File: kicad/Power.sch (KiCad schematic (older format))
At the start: 11 parts, among them P3 Battery, U3 LXDC2URxx

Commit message: 自動配線成功
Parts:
- P3: footprint Connectors_Hirose:Hirose_DF13-02P-1.25DSA_02x1.25mm_Straight -> mouse:Hirose_DF13-02P-1.25DSA_02x1.25mm_Straight
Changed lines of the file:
@@
 F 0 "P3" H 1700 4600 50  0000 C CNN
 F 1 "Battery" V 1800 4450 50  0000 C CNN
-F 2 "Connectors_Hirose:Hirose_DF13-02P-1.25DSA_02x1.25mm_Straight" H 1700 4450 50  0001 C CNN
+F 2 "mouse:Hirose_DF13-02P-1.25DSA_02x1.25mm_Straight" H 1700 4450 50  0001 C CNN
 F 3 "" H 1700 4450 50  0000 C CNN
 	1    1700 4450

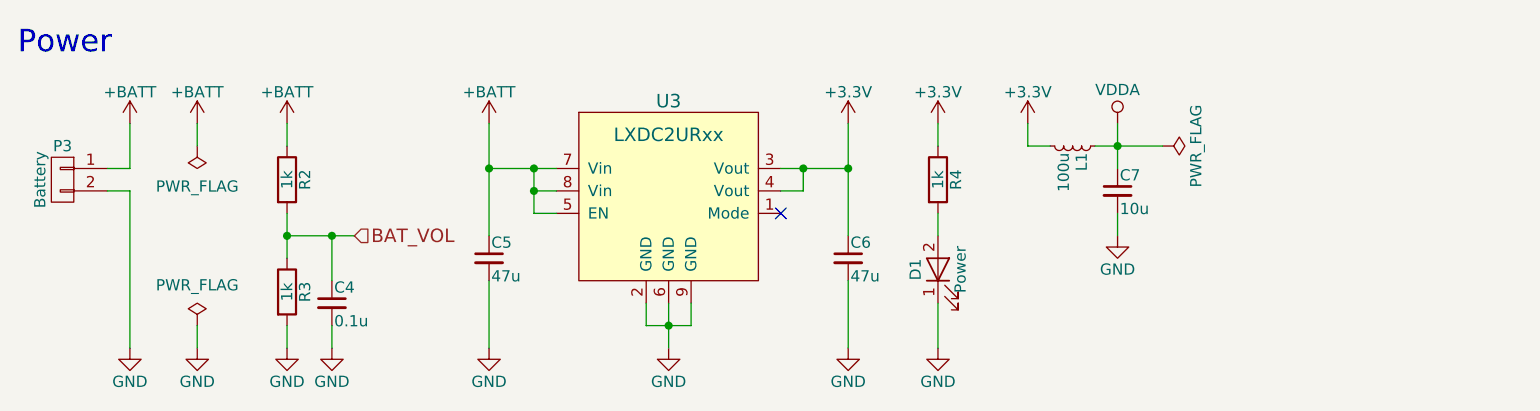
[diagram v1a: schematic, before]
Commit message: 回路を改良
受光部をフォトトランジスタに変更
測距センサをVL6180Xに変更
動作電圧を3Vに変更
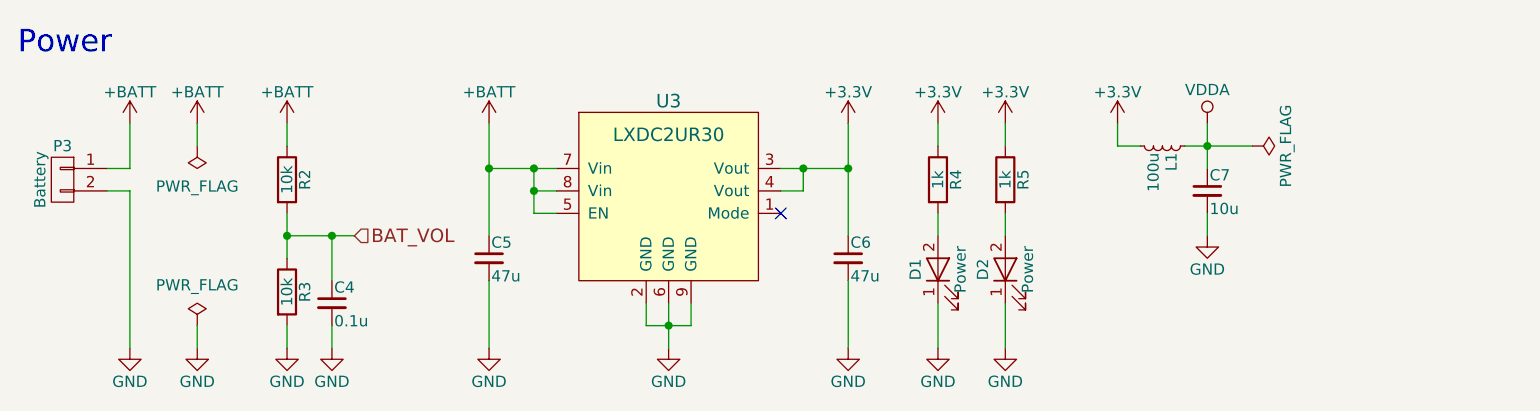
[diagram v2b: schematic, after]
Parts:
- added D2: Power, LEDs:LED_0402, symbol LED
- added R5: 1k, Resistors_SMD:R_0201, symbol R
- R2, R3: value 1k -> 10k
- U3: value LXDC2URxx -> LXDC2UR30
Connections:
- net +3V3: now also R5.1
- net GND: now also D2.1 (K)
- new net: D2.2 (A), R5.2
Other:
- moved on the sheet: C7, L1
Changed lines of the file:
@@
 LIBS:ftdi
 LIBS:gennum
-LIBS:graphic
 LIBS:hc11
 LIBS:ir
 LIBS:Lattice
 LIBS:leds
-LIBS:logo
 LIBS:maxim
 LIBS:mechanical
@@
 LIBS:zetex
 LIBS:Zilog
+LIBS:graphic_symbols
+LIBS:infineon
+LIBS:intersil
+LIBS:LEM
+LIBS:logic_programmable
+LIBS:RFSolutions
 LIBS:KERISE-cache
 EELAYER 25 0
@@
 P 2700 4450
 F 0 "R2" V 2780 4450 50  0000 C CNN
-F 1 "1k" V 2700 4450 50  0000 C CNN
+F 1 "10k" V 2700 4450 50  0000 C CNN
 F 2 "Resistors_SMD:R_0201" V 2630 4450 50  0001 C CNN
 F 3 "" H 2700 4450 50  0000 C CNN
@@
 P 2700 4950
 F 0 "R3" V 2780 4950 50  0000 C CNN
-F 1 "1k" V 2700 4950 50  0000 C CNN
+F 1 "10k" V 2700 4950 50  0000 C CNN
 F 2 "Resistors_SMD:R_0201" V 2630 4950 50  0001 C CNN
 F 3 "" H 2700 4950 50  0000 C CNN
@@
 P 4400 4250
 F 0 "U3" H 4400 4400 60  0000 C CNN
-F 1 "LXDC2URxx" H 4400 4250 60  0000 C CNN
+F 1 "LXDC2UR30" H 4400 4250 60  0000 C CNN
 F 2 "mouse:LXDC2UR" H 4400 4250 60  0001 C CNN
 F 3 "" H 4400 4250 60  0000 C CNN
@@
 L +3.3V #PWR031
 U 1 1 59C37023
-P 6000 4200
-F 0 "#PWR031" H 6000 4050 50  0001 C CNN
-F 1 "+3.3V" H 6000 4340 50  0000 C CNN
-F 2 "" H 6000 4200 50  0001 C CNN
-F 3 "" H 6000 4200 50  0001 C CNN
-	1    6000 4200
-	1    0    0    -1
-$EndComp
-$Comp
-L VDDA #PWR032
-U 1 1 59C37047
 P 6400 4200
-F 0 "#PWR032" H 6400 4050 50  0001 C CNN
-F 1 "VDDA" H 6400 4350 50  0000 C CNN
+F 0 "#PWR031" H 6400 4050 50  0001 C CNN
+F 1 "+3.3V" H 6400 4340 50  0000 C CNN
 F 2 "" H 6400 4200 50  0001 C CNN
 F 3 "" H 6400 4200 50  0001 C CNN
@@
 $EndComp
 $Comp
+L VDDA #PWR032
+U 1 1 59C37047
+P 6800 4200
+F 0 "#PWR032" H 6800 4050 50  0001 C CNN
+F 1 "VDDA" H 6800 4350 50  0000 C CNN
+F 2 "" H 6800 4200 50  0001 C CNN
+F 3 "" H 6800 4200 50  0001 C CNN
+	1    6800 4200
+	1    0    0    -1
+$EndComp
+$Comp
 L L_Small L1
 U 1 1 59C3706B
-P 6200 4300
-F 0 "L1" H 6230 4340 50  0000 L CNN
-F 1 "100u" H 6230 4260 50  0000 L CNN
-F 2 "Capacitors_SMD:C_0603" H 6200 4300 50  0001 C CNN
-F 3 "" H 6200 4300 50  0001 C CNN
-	1    6200 4300
+P 6600 4300
+F 0 "L1" H 6630 4340 50  0000 L CNN
+F 1 "100u" H 6630 4260 50  0000 L CNN
+F 2 "Capacitors_SMD:C_0603" H 6600 4300 50  0001 C CNN
+F 3 "" H 6600 4300 50  0001 C CNN
+	1    6600 4300
 	0    1    1    0
 $EndComp
@@
 L C_Small C7
 U 1 1 59C370C1
-P 6400 4500
-F 0 "C7" H 6410 4570 50  0000 L CNN
-F 1 "10u" H 6410 4420 50  0000 L CNN
-F 2 "Capacitors_SMD:C_0402" H 6400 4500 50  0001 C CNN
-F 3 "" H 6400 4500 50  0001 C CNN
-	1    6400 4500
-	1    0    0    -1
-$EndComp
-Wire Wire Line
-	6400 4200 6400 4400
+P 6800 4500
+F 0 "C7" H 6810 4570 50  0000 L CNN
+F 1 "10u" H 6810 4420 50  0000 L CNN
+F 2 "Capacitors_SMD:C_0402" H 6800 4500 50  0001 C CNN
+F 3 "" H 6800 4500 50  0001 C CNN
+	1    6800 4500
+	1    0    0    -1
+$EndComp
+Wire Wire Line
+	6800 4200 6800 4400
 $Comp
 L GND #PWR033
 U 1 1 59C37170
-P 6400 4700
-F 0 "#PWR033" H 6400 4450 50  0001 C CNN
-F 1 "GND" H 6400 4550 50  0000 C CNN
-F 2 "" H 6400 4700 50  0000 C CNN
-F 3 "" H 6400 4700 50  0000 C CNN
-	1    6400 4700
-	1    0    0    -1
-$EndComp
-Wire Wire Line
-	6400 4700 6400 4600
-Wire Wire Line
-	6300 4300 6600 4300
-Connection ~ 6400 4300
-Wire Wire Line
-	6100 4300 6000 4300
-Wire Wire Line
-	6000 4300 6000 4200
+P 6800 4700
+F 0 "#PWR033" H 6800 4450 50  0001 C CNN
+F 1 "GND" H 6800 4550 50  0000 C CNN
+F 2 "" H 6800 4700 50  0000 C CNN
+F 3 "" H 6800 4700 50  0000 C CNN
+	1    6800 4700
+	1    0    0    -1
+$EndComp
+Wire Wire Line
+	6800 4700 6800 4600
+Wire Wire Line
+	6700 4300 7000 4300
+Connection ~ 6800 4300
+Wire Wire Line
+	6500 4300 6400 4300
+Wire Wire Line
+	6400 4300 6400 4200
 $Comp
 L C_Small C5
@@
 L PWR_FLAG #FLG035
 U 1 1 5A1BE075
-P 6600 4300
-F 0 "#FLG035" H 6600 4375 50  0001 C CNN
-F 1 "PWR_FLAG" H 6600 4450 50  0000 C CNN
-F 2 "" H 6600 4300 50  0001 C CNN
-F 3 "" H 6600 4300 50  0001 C CNN
-	1    6600 4300
+P 7000 4300
+F 0 "#FLG035" H 7000 4375 50  0001 C CNN
+F 1 "PWR_FLAG" H 7000 4450 50  0000 C CNN
+F 2 "" H 7000 4300 50  0001 C CNN
+F 3 "" H 7000 4300 50  0001 C CNN
+	1    7000 4300
 	0    1    1    0
 $EndComp
+$Comp
+L R R5
+U 1 1 5A4BB521
+P 5900 4450
+F 0 "R5" V 5980 4450 50  0000 C CNN
+F 1 "1k" V 5900 4450 50  0000 C CNN
+F 2 "Resistors_SMD:R_0201" V 5830 4450 50  0001 C CNN
+F 3 "" H 5900 4450 50  0000 C CNN
+	1    5900 4450
+	1    0    0    -1
+$EndComp
+$Comp
+L GND #PWR036
+U 1 1 5A4BB527
+P 5900 5200
+F 0 "#PWR036" H 5900 4950 50  0001 C CNN
+F 1 "GND" H 5900 5050 50  0000 C CNN
+F 2 "" H 5900 5200 50  0000 C CNN
+F 3 "" H 5900 5200 50  0000 C CNN
+	1    5900 5200
+	1    0    0    -1
+$EndComp
+$Comp
+L +3.3V #PWR037
+U 1 1 5A4BB52D
+P 5900 4200
+F 0 "#PWR037" H 5900 4050 50  0001 C CNN
+F 1 "+3.3V" H 5900 4340 50  0000 C CNN
+F 2 "" H 5900 4200 50  0000 C CNN
+F 3 "" H 5900 4200 50  0000 C CNN
+	1    5900 4200
+	1    0    0    -1
+$EndComp
+Wire Wire Line
+	5900 4700 5900 4600
+Wire Wire Line
+	5900 4300 5900 4200
+$Comp
+L LED D2
+U 1 1 5A4BB535
+P 5900 4850
+F 0 "D2" H 5900 4950 50  0000 C CNN
+F 1 "Power" H 5900 4750 50  0000 C CNN
+F 2 "LEDs:LED_0402" H 5900 4850 50  0001 C CNN
+F 3 "" H 5900 4850 50  0001 C CNN
+	1    5900 4850
+	0    -1   -1   0
+$EndComp
+Wire Wire Line
+	5900 5000 5900 5200
 $EndSCHEMATC

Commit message: 部品を配置
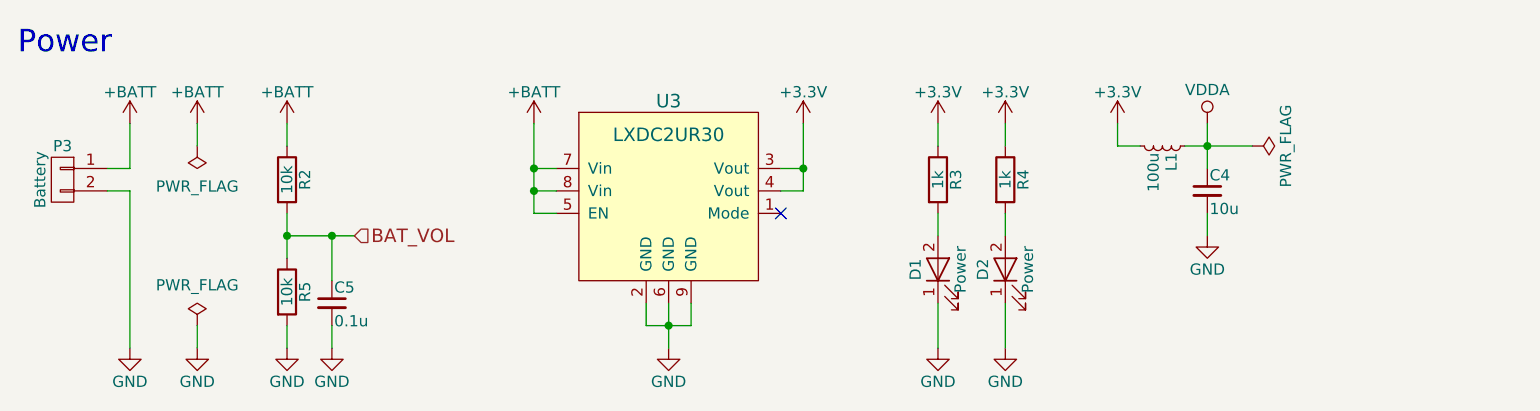
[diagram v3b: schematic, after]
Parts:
- removed C5, C6: 47u, Capacitors_SMD:C_0805, symbol C_Small
- C4: renamed from C7; footprint Capacitors_SMD:C_0402 -> Capacitors_SMD:C_0402_NoSilk
- C5: renamed from C4; footprint Capacitors_SMD:C_0201 -> Capacitors_SMD:C_0201_NoSilk
- R2: footprint Resistors_SMD:R_0201 -> Resistors_SMD:R_0201_NoSilk
- R3: renamed from R4; footprint Resistors_SMD:R_0201 -> Resistors_SMD:R_0201_NoSilk
- R4: renamed from R5; footprint Resistors_SMD:R_0201 -> Resistors_SMD:R_0201_NoSilk
- R5: renamed from R3; footprint Resistors_SMD:R_0201 -> Resistors_SMD:R_0201_NoSilk
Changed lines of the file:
@@
 $Descr A4 11693 8268
 encoding utf-8
-Sheet 3 15
+Sheet 3 16
 Title ""
 Date ""
@@
 F 0 "R2" V 2780 4450 50  0000 C CNN
 F 1 "10k" V 2700 4450 50  0000 C CNN
-F 2 "Resistors_SMD:R_0201" V 2630 4450 50  0001 C CNN
+F 2 "Resistors_SMD:R_0201_NoSilk" V 2630 4450 50  0001 C CNN
 F 3 "" H 2700 4450 50  0000 C CNN
 	1    2700 4450
@@
 $EndComp
 $Comp
-L R R3
+L R R5
 U 1 1 57CD3B95
 P 2700 4950
-F 0 "R3" V 2780 4950 50  0000 C CNN
+F 0 "R5" V 2780 4950 50  0000 C CNN
 F 1 "10k" V 2700 4950 50  0000 C CNN
-F 2 "Resistors_SMD:R_0201" V 2630 4950 50  0001 C CNN
+F 2 "Resistors_SMD:R_0201_NoSilk" V 2630 4950 50  0001 C CNN
 F 3 "" H 2700 4950 50  0000 C CNN
 	1    2700 4950
@@
 $EndComp
 $Comp
-L R R4
+L R R3
 U 1 1 57D00960
 P 5600 4450
-F 0 "R4" V 5680 4450 50  0000 C CNN
+F 0 "R3" V 5680 4450 50  0000 C CNN
 F 1 "1k" V 5600 4450 50  0000 C CNN
-F 2 "Resistors_SMD:R_0201" V 5530 4450 50  0001 C CNN
+F 2 "Resistors_SMD:R_0201_NoSilk" V 5530 4450 50  0001 C CNN
 F 3 "" H 5600 4450 50  0000 C CNN
 	1    5600 4450
@@
 L +BATT #PWR025
 U 1 1 592A5000
-P 3600 4200
-F 0 "#PWR025" H 3600 4050 50  0001 C CNN
-F 1 "+BATT" H 3600 4340 50  0000 C CNN
-F 2 "" H 3600 4200 50  0000 C CNN
-F 3 "" H 3600 4200 50  0000 C CNN
-	1    3600 4200
+P 3800 4200
+F 0 "#PWR025" H 3800 4050 50  0001 C CNN
+F 1 "+BATT" H 3800 4340 50  0000 C CNN
+F 2 "" H 3800 4200 50  0000 C CNN
+F 3 "" H 3800 4200 50  0000 C CNN
+	1    3800 4200
 	1    0    0    -1
 $EndComp
@@
 L +3.3V #PWR027
 U 1 1 592A5664
-P 5200 4200
-F 0 "#PWR027" H 5200 4050 50  0001 C CNN
-F 1 "+3.3V" H 5200 4340 50  0000 C CNN
-F 2 "" H 5200 4200 50  0000 C CNN
-F 3 "" H 5200 4200 50  0000 C CNN
-	1    5200 4200
+P 5000 4200
+F 0 "#PWR027" H 5000 4050 50  0001 C CNN
+F 1 "+3.3V" H 5000 4340 50  0000 C CNN
+F 2 "" H 5000 4200 50  0000 C CNN
+F 3 "" H 5000 4200 50  0000 C CNN
+	1    5000 4200
 	1    0    0    -1
 $EndComp
 NoConn ~ 4900 4600
 $Comp
-L C_Small C6
-U 1 1 592A5C4A
-P 5200 4800
-F 0 "C6" H 5210 4870 50  0000 L CNN
-F 1 "47u" H 5210 4720 50  0000 L CNN
-F 2 "Capacitors_SMD:C_0805" H 5200 4800 50  0001 C CNN
-F 3 "" H 5200 4800 50  0000 C CNN
-	1    5200 4800
-	1    0    0    -1
-$EndComp
-$Comp
 L GND #PWR028
-U 1 1 592A5C9B
-P 5200 5200
-F 0 "#PWR028" H 5200 4950 50  0001 C CNN
-F 1 "GND" H 5200 5050 50  0000 C CNN
-F 2 "" H 5200 5200 50  0000 C CNN
-F 3 "" H 5200 5200 50  0000 C CNN
-	1    5200 5200
-	1    0    0    -1
-$EndComp
-$Comp
-L GND #PWR029
 U 1 1 57CC113A
 P 2000 5200
-F 0 "#PWR029" H 2000 4950 50  0001 C CNN
+F 0 "#PWR028" H 2000 4950 50  0001 C CNN
 F 1 "GND" H 2000 5050 50  0000 C CNN
 F 2 "" H 2000 5200 50  0000 C CNN
@@
 	2000 4400 1900 4400
 Wire Wire Line
-	3600 4400 3900 4400
-Wire Wire Line
-	3600 4200 3600 4700
-Wire Wire Line
 	3900 4500 3800 4500
 Wire Wire Line
-	3800 4400 3800 4600
+	3800 4200 3800 4600
 Connection ~ 3800 4400
 Wire Wire Line
@@
 	4500 5100 4500 5000
 Wire Wire Line
-	5200 4200 5200 4700
-Wire Wire Line
-	4900 4400 5200 4400
-Wire Wire Line
-	4900 4500 5000 4500
-Wire Wire Line
-	5000 4500 5000 4400
+	5000 4500 4900 4500
+Wire Wire Line
+	5000 4200 5000 4500
 Connection ~ 5000 4400
 Wire Wire Line
-	5200 5200 5200 4900
-Connection ~ 5200 4400
-Wire Wire Line
 	2000 4200 2000 4400
-$Comp
-L GND #PWR030
-U 1 1 593DFA5D
-P 3600 5200
-F 0 "#PWR030" H 3600 4950 50  0001 C CNN
-F 1 "GND" H 3600 5050 50  0000 C CNN
-F 2 "" H 3600 5200 50  0000 C CNN
-F 3 "" H 3600 5200 50  0000 C CNN
-	1    3600 5200
-	1    0    0    -1
-$EndComp
-Wire Wire Line
-	3600 5200 3600 4900
-Connection ~ 3600 4400
 $Comp
 L LED D1
@@
 	5600 5000 5600 5200
 $Comp
-L +3.3V #PWR031
+L +3.3V #PWR029
 U 1 1 59C37023
 P 6400 4200
-F 0 "#PWR031" H 6400 4050 50  0001 C CNN
+F 0 "#PWR029" H 6400 4050 50  0001 C CNN
 F 1 "+3.3V" H 6400 4340 50  0000 C CNN
 F 2 "" H 6400 4200 50  0001 C CNN
@@
 $EndComp
 $Comp
-L VDDA #PWR032
+L VDDA #PWR030
 U 1 1 59C37047
 P 6800 4200
-F 0 "#PWR032" H 6800 4050 50  0001 C CNN
+F 0 "#PWR030" H 6800 4050 50  0001 C CNN
 F 1 "VDDA" H 6800 4350 50  0000 C CNN
 F 2 "" H 6800 4200 50  0001 C CNN
@@
 $EndComp
 $Comp
-L C_Small C7
+L C_Small C4
 U 1 1 59C370C1
 P 6800 4500
-F 0 "C7" H 6810 4570 50  0000 L CNN
+F 0 "C4" H 6810 4570 50  0000 L CNN
 F 1 "10u" H 6810 4420 50  0000 L CNN
-F 2 "Capacitors_SMD:C_0402" H 6800 4500 50  0001 C CNN
+F 2 "Capacitors_SMD:C_0402_NoSilk" H 6800 4500 50  0001 C CNN
 F 3 "" H 6800 4500 50  0001 C CNN
 	1    6800 4500
@@
 	6800 4200 6800 4400
 $Comp
-L GND #PWR033
+L GND #PWR031
 U 1 1 59C37170
 P 6800 4700
-F 0 "#PWR033" H 6800 4450 50  0001 C CNN
+F 0 "#PWR031" H 6800 4450 50  0001 C CNN
 F 1 "GND" H 6800 4550 50  0000 C CNN
 F 2 "" H 6800 4700 50  0000 C CNN
@@
 $Comp
 L C_Small C5
-U 1 1 59C37F58
-P 3600 4800
-F 0 "C5" H 3610 4870 50  0000 L CNN
-F 1 "47u" H 3610 4720 50  0000 L CNN
-F 2 "Capacitors_SMD:C_0805" H 3600 4800 50  0001 C CNN
-F 3 "" H 3600 4800 50  0000 C CNN
-	1    3600 4800
-	1    0    0    -1
-$EndComp
-$Comp
-L C_Small C4
 U 1 1 59C47577
 P 2900 5000
-F 0 "C4" H 2910 5070 50  0000 L CNN
+F 0 "C5" H 2910 5070 50  0000 L CNN
 F 1 "0.1u" H 2910 4920 50  0000 L CNN
-F 2 "Capacitors_SMD:C_0201" H 2900 5000 50  0001 C CNN
+F 2 "Capacitors_SMD:C_0201_NoSilk" H 2900 5000 50  0001 C CNN
 F 3 "" H 2900 5000 50  0001 C CNN
 	1    2900 5000
@@
 $EndComp
 $Comp
-L GND #PWR034
+L GND #PWR032
 U 1 1 59C475E6
 P 2900 5200
-F 0 "#PWR034" H 2900 4950 50  0001 C CNN
+F 0 "#PWR032" H 2900 4950 50  0001 C CNN
 F 1 "GND" H 2900 5050 50  0000 C CNN
 F 2 "" H 2900 5200 50  0000 C CNN
@@
 	2900 5100 2900 5200
 $Comp
-L PWR_FLAG #FLG035
+L PWR_FLAG #FLG033
 U 1 1 5A1BE075
 P 7000 4300
-F 0 "#FLG035" H 7000 4375 50  0001 C CNN
+F 0 "#FLG033" H 7000 4375 50  0001 C CNN
 F 1 "PWR_FLAG" H 7000 4450 50  0000 C CNN
 F 2 "" H 7000 4300 50  0001 C CNN
@@
 $EndComp
 $Comp
-L R R5
+L R R4
 U 1 1 5A4BB521
 P 5900 4450
-F 0 "R5" V 5980 4450 50  0000 C CNN
+F 0 "R4" V 5980 4450 50  0000 C CNN
 F 1 "1k" V 5900 4450 50  0000 C CNN
-F 2 "Resistors_SMD:R_0201" V 5830 4450 50  0001 C CNN
+F 2 "Resistors_SMD:R_0201_NoSilk" V 5830 4450 50  0001 C CNN
 F 3 "" H 5900 4450 50  0000 C CNN
 	1    5900 4450
@@
 $EndComp
 $Comp
-L GND #PWR036
+L GND #PWR034
 U 1 1 5A4BB527
 P 5900 5200
-F 0 "#PWR036" H 5900 4950 50  0001 C CNN
+F 0 "#PWR034" H 5900 4950 50  0001 C CNN
 F 1 "GND" H 5900 5050 50  0000 C CNN
 F 2 "" H 5900 5200 50  0000 C CNN
@@
 $EndComp
 $Comp
-L +3.3V #PWR037
+L +3.3V #PWR035
 U 1 1 5A4BB52D
 P 5900 4200
-F 0 "#PWR037" H 5900 4050 50  0001 C CNN
+F 0 "#PWR035" H 5900 4050 50  0001 C CNN
 F 1 "+3.3V" H 5900 4340 50  0000 C CNN
 F 2 "" H 5900 4200 50  0000 C CNN
@@
 Wire Wire Line
 	5900 5000 5900 5200
+Wire Wire Line
+	5000 4400 4900 4400
+Wire Wire Line
+	3900 4400 3800 4400
 $EndSCHEMATC

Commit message: 回路を編集 ToFを除去
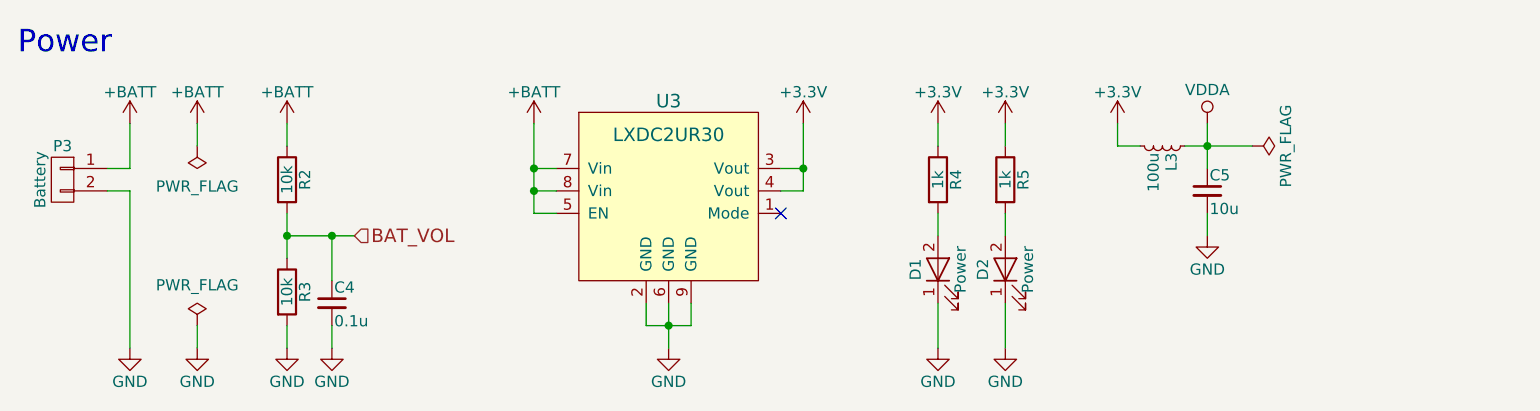
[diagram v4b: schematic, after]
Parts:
- renumbered C5 to C4, C4 to C5, L1 to L3, R5 to R3, R3 to R4, R4 to R5
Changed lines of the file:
@@
 $Descr A4 11693 8268
 encoding utf-8
-Sheet 3 16
+Sheet 3 15
 Title ""
 Date ""
@@
 $EndComp
 $Comp
-L R R5
+L R R3
 U 1 1 57CD3B95
 P 2700 4950
-F 0 "R5" V 2780 4950 50  0000 C CNN
+F 0 "R3" V 2780 4950 50  0000 C CNN
 F 1 "10k" V 2700 4950 50  0000 C CNN
 F 2 "Resistors_SMD:R_0201_NoSilk" V 2630 4950 50  0001 C CNN
@@
 $EndComp
 $Comp
-L R R3
+L R R4
 U 1 1 57D00960
 P 5600 4450
-F 0 "R3" V 5680 4450 50  0000 C CNN
+F 0 "R4" V 5680 4450 50  0000 C CNN
 F 1 "1k" V 5600 4450 50  0000 C CNN
 F 2 "Resistors_SMD:R_0201_NoSilk" V 5530 4450 50  0001 C CNN
@@
 $EndComp
 $Comp
-L L_Small L1
+L L_Small L3
 U 1 1 59C3706B
 P 6600 4300
-F 0 "L1" H 6630 4340 50  0000 L CNN
+F 0 "L3" H 6630 4340 50  0000 L CNN
 F 1 "100u" H 6630 4260 50  0000 L CNN
 F 2 "Capacitors_SMD:C_0603" H 6600 4300 50  0001 C CNN
@@
 $EndComp
 $Comp
-L C_Small C4
+L C_Small C5
 U 1 1 59C370C1
 P 6800 4500
-F 0 "C4" H 6810 4570 50  0000 L CNN
+F 0 "C5" H 6810 4570 50  0000 L CNN
 F 1 "10u" H 6810 4420 50  0000 L CNN
 F 2 "Capacitors_SMD:C_0402_NoSilk" H 6800 4500 50  0001 C CNN
@@
 	6400 4300 6400 4200
 $Comp
-L C_Small C5
+L C_Small C4
 U 1 1 59C47577
 P 2900 5000
-F 0 "C5" H 2910 5070 50  0000 L CNN
+F 0 "C4" H 2910 5070 50  0000 L CNN
 F 1 "0.1u" H 2910 4920 50  0000 L CNN
 F 2 "Capacitors_SMD:C_0201_NoSilk" H 2900 5000 50  0001 C CNN
@@
 $EndComp
 $Comp
-L R R4
+L R R5
 U 1 1 5A4BB521
 P 5900 4450
-F 0 "R4" V 5980 4450 50  0000 C CNN
+F 0 "R5" V 5980 4450 50  0000 C CNN
 F 1 "1k" V 5900 4450 50  0000 C CNN
 F 2 "Resistors_SMD:R_0201_NoSilk" V 5830 4450 50  0001 C CNN

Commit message: 部品を配置 kicad5
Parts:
- removed P3: Battery, mouse:Hirose_DF13-02P-1.25DSA_02x1.25mm_Straight, symbol CONN_01X02
- added BT1: Battery, mouse:Hirose_DF13-02P-1.25DSA_02x1.25mm_Straight, symbol Device:Battery_Cell
- C4, C5: symbol C_Small -> Device:C_Small
- D1, D2: symbol LED -> Device:LED
- L3: symbol L_Small -> Device:L_Small
- R2, R3, R4, R5: symbol R -> Device:R
- U3: symbol LXDC2URxx -> KERISE:LXDC2URxx
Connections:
- net +BATT: now also BT1.1 (+)
- net GND: now also BT1.2 (-)
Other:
- moved on the sheet: C4, C5, L3, R2, R3, R4, R5, U3
